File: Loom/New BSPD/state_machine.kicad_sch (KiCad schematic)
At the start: 9 parts, among them U1 4011, U11 4012, U12 74LS573, U3 4011, U4 4011, U5 4011, U6 4011, U7 4011, U8 4011

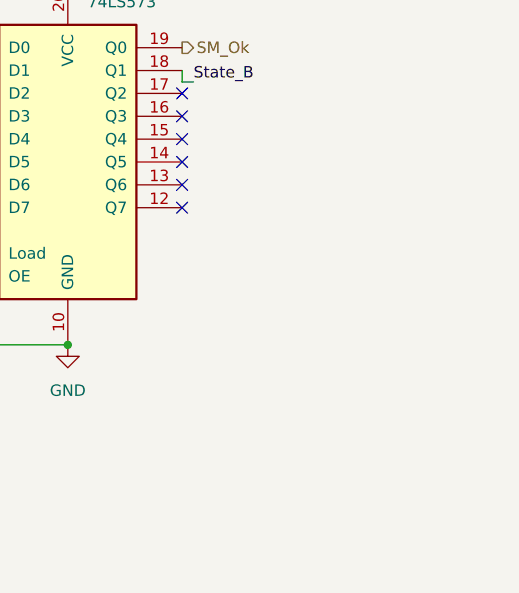
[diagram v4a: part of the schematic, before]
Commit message: Add State, Shutdown LEDs, Complete rough board layout
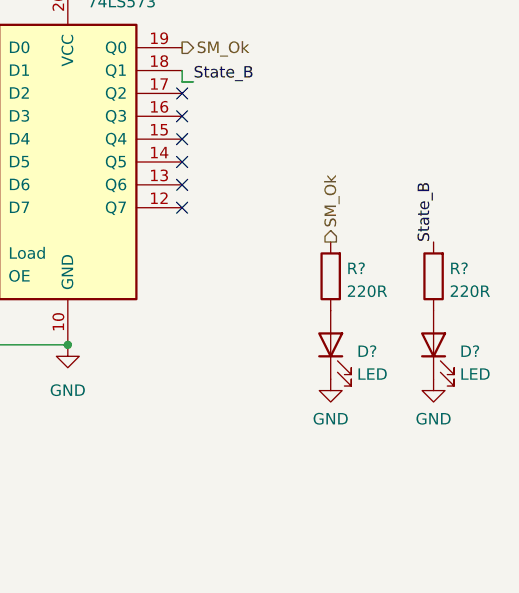
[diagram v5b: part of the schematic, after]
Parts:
- added D? (x2): LED, LED_THT:LED_D5.0mm, symbol Device:LED
- added R? (x2): 220R, Resistor_THT:R_Axial_DIN0207_L6.3mm_D2.5mm_P7.62mm_Horizontal, symbol Device:R
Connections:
- net GND: now also D?.1 (K), D?.1 (K)
- net SM_Ok: now also R?.2
- net State_B: now also R?.2
- new net: D?.2 (A), R?.1 (x2)
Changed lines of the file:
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@@
     (effects (font (size 1.27 1.27)) (justify right bottom))
+  )
+  (label "State_B" (at 264.16 72.39 90) (fields_autoplaced)
+    (effects (font (size 1.27 1.27)) (justify left bottom))
   )
   (label "State_B" (at 113.03 71.12 180) (fields_autoplaced)
@@
     (effects (font (size 1.27 1.27)) (justify right))
   )
+  (hierarchical_label "SM_Ok" (shape output) (at 252.73 72.39 90) (fields_autoplaced)
+    (effects (font (size 1.27 1.27)) (justify left))
+  )
   (hierarchical_label "SM_Ok" (shape output) (at 113.03 74.93 180) (fields_autoplaced)
     (effects (font (size 1.27 1.27)) (justify right))
@@
     )
   )
+  (symbol (lib_id "Device:R") (at 252.73 76.2 180) (unit 1)
+    (in_bom yes) (on_board yes) (dnp no) (fields_autoplaced)
+    (property "Reference" "R?" (at 254.508 75.3653 0)
+      (effects (font (size 1.27 1.27)) (justify right))
+    )
+    (property "Value" "220R" (at 254.508 77.9022 0)
+      (effects (font (size 1.27 1.27)) (justify right))
+    )
+    (property "Footprint" "Resistor_THT:R_Axial_DIN0207_L6.3mm_D2.5mm_P7.62mm_Horizontal" (at 254.508 76.2 90)
+      (effects (font (size 1.27 1.27)) hide)
+    )
+    (property "Datasheet" "~" (at 252.73 76.2 0)
+      (effects (font (size 1.27 1.27)) hide)
+    )
+    (pin "1")
+    (pin "2")
+    (instances
+      (project "New BSPD"
+        (path "/1f7c501a-057f-4634-92ce-528b01503799"
+          (reference "R?") (unit 1)
+        )
+        (path "/1f7c501a-057f-4634-92ce-528b01503799/81a2d232-b56a-457d-8f4d-f7bde46d944b"
+          (reference "R7") (unit 1)
+        )
+        (path "/1f7c501a-057f-4634-92ce-528b01503799/c1af1d02-f1c8-42b8-8d3c-ac3883e05aae"
+          (reference "R9") (unit 1)
+        )
+      )
+      (project "BSPD - FSG"
+        (path "/ea40ab7b-80c4-4cf6-acf9-83a05b0cd5a6"
+          (reference "R?") (unit 1)
+        )
+      )
+    )
+  )
   (symbol (lib_id "4xxx:4011") (at 55.88 139.7 0) (unit 4)
     (in_bom yes) (on_board yes) (dnp no) (fields_autoplaced)
@@
     )
   )
+  (symbol (lib_id "Device:LED") (at 264.16 83.82 90) (unit 1)
+    (in_bom yes) (on_board yes) (dnp no) (fields_autoplaced)
+    (property "Reference" "D?" (at 267.081 84.5728 90)
+      (effects (font (size 1.27 1.27)) (justify right))
+    )
+    (property "Value" "LED" (at 267.081 87.1097 90)
+      (effects (font (size 1.27 1.27)) (justify right))
+    )
+    (property "Footprint" "LED_THT:LED_D5.0mm" (at 264.16 83.82 0)
+      (effects (font (size 1.27 1.27)) hide)
+    )
+    (property "Datasheet" "~" (at 264.16 83.82 0)
+      (effects (font (size 1.27 1.27)) hide)
+    )
+    (pin "1")
+    (pin "2")
+    (instances
+      (project "New BSPD"
+        (path "/1f7c501a-057f-4634-92ce-528b01503799"
+          (reference "D?") (unit 1)
+        )
+        (path "/1f7c501a-057f-4634-92ce-528b01503799/81a2d232-b56a-457d-8f4d-f7bde46d944b"
+          (reference "D5") (unit 1)
+        )
+        (path "/1f7c501a-057f-4634-92ce-528b01503799/c1af1d02-f1c8-42b8-8d3c-ac3883e05aae"
+          (reference "D7") (unit 1)
+        )
+      )
+      (project "BSPD - FSG"
+        (path "/ea40ab7b-80c4-4cf6-acf9-83a05b0cd5a6"
+          (reference "D?") (unit 1)
+        )
+      )
+    )
+  )
   (symbol (lib_id "power:+5V") (at 171.45 21.59 0) (unit 1)
     (in_bom yes) (on_board yes) (dnp no) (fields_autoplaced)
@@
     )
   )
+  (symbol (lib_id "power:GND") (at 252.73 87.63 0) (unit 1)
+    (in_bom yes) (on_board yes) (dnp no) (fields_autoplaced)
+    (property "Reference" "#PWR?" (at 252.73 93.98 0)
+      (effects (font (size 1.27 1.27)) hide)
+    )
+    (property "Value" "GND" (at 252.73 92.0734 0)
+      (effects (font (size 1.27 1.27)))
+    )
+    (property "Footprint" "" (at 252.73 87.63 0)
+      (effects (font (size 1.27 1.27)) hide)
+    )
+    (property "Datasheet" "" (at 252.73 87.63 0)
+      (effects (font (size 1.27 1.27)) hide)
+    )
+    (pin "1")
+    (instances
+      (project "New BSPD"
+        (path "/1f7c501a-057f-4634-92ce-528b01503799"
+          (reference "#PWR?") (unit 1)
+        )
+        (path "/1f7c501a-057f-4634-92ce-528b01503799/81a2d232-b56a-457d-8f4d-f7bde46d944b"
+          (reference "#PWR022") (unit 1)
+        )
+        (path "/1f7c501a-057f-4634-92ce-528b01503799/c1af1d02-f1c8-42b8-8d3c-ac3883e05aae"
+          (reference "#PWR044") (unit 1)
+        )
+      )
+      (project "BSPD - FSG"
+        (path "/ea40ab7b-80c4-4cf6-acf9-83a05b0cd5a6"
+          (reference "#PWR?") (unit 1)
+        )
+      )
+    )
+  )
   (symbol (lib_id "power:+5V") (at 134.62 31.75 0) (unit 1)
     (in_bom yes) (on_board yes) (dnp no) (fields_autoplaced)
@@
     )
   )
+  (symbol (lib_id "Device:R") (at 264.16 76.2 180) (unit 1)
+    (in_bom yes) (on_board yes) (dnp no) (fields_autoplaced)
+    (property "Reference" "R?" (at 265.938 75.3653 0)
+      (effects (font (size 1.27 1.27)) (justify right))
+    )
+    (property "Value" "220R" (at 265.938 77.9022 0)
+      (effects (font (size 1.27 1.27)) (justify right))
+    )
+    (property "Footprint" "Resistor_THT:R_Axial_DIN0207_L6.3mm_D2.5mm_P7.62mm_Horizontal" (at 265.938 76.2 90)
+      (effects (font (size 1.27 1.27)) hide)
+    )
+    (property "Datasheet" "~" (at 264.16 76.2 0)
+      (effects (font (size 1.27 1.27)) hide)
+    )
+    (pin "1")
+    (pin "2")
+    (instances
+      (project "New BSPD"
+        (path "/1f7c501a-057f-4634-92ce-528b01503799"
+          (reference "R?") (unit 1)
+        )
+        (path "/1f7c501a-057f-4634-92ce-528b01503799/81a2d232-b56a-457d-8f4d-f7bde46d944b"
+          (reference "R7") (unit 1)
+        )
+        (path "/1f7c501a-057f-4634-92ce-528b01503799/c1af1d02-f1c8-42b8-8d3c-ac3883e05aae"
+          (reference "R10") (unit 1)
+        )
+      )
+      (project "BSPD - FSG"
+        (path "/ea40ab7b-80c4-4cf6-acf9-83a05b0cd5a6"
+          (reference "R?") (unit 1)
+        )
+      )
+    )
+  )
   (symbol (lib_id "4xxx:4011") (at 166.37 71.12 0) (unit 3)
     (in_bom yes) (on_board yes) (dnp no) (fields_autoplaced)
@@
     )
   )
+  (symbol (lib_id "power:GND") (at 264.16 87.63 0) (unit 1)
+    (in_bom yes) (on_board yes) (dnp no) (fields_autoplaced)
+    (property "Reference" "#PWR?" (at 264.16 93.98 0)
+      (effects (font (size 1.27 1.27)) hide)
+    )
+    (property "Value" "GND" (at 264.16 92.0734 0)
+      (effects (font (size 1.27 1.27)))
+    )
+    (property "Footprint" "" (at 264.16 87.63 0)
+      (effects (font (size 1.27 1.27)) hide)
+    )
+    (property "Datasheet" "" (at 264.16 87.63 0)
+      (effects (font (size 1.27 1.27)) hide)
+    )
+    (pin "1")
+    (instances
+      (project "New BSPD"
+        (path "/1f7c501a-057f-4634-92ce-528b01503799"
+          (reference "#PWR?") (unit 1)
+        )
+        (path "/1f7c501a-057f-4634-92ce-528b01503799/81a2d232-b56a-457d-8f4d-f7bde46d944b"
+          (reference "#PWR022") (unit 1)
+        )
+        (path "/1f7c501a-057f-4634-92ce-528b01503799/c1af1d02-f1c8-42b8-8d3c-ac3883e05aae"
+          (reference "#PWR045") (unit 1)
+        )
+      )
+      (project "BSPD - FSG"
+        (path "/ea40ab7b-80c4-4cf6-acf9-83a05b0cd5a6"
+          (reference "#PWR?") (unit 1)
+        )
+      )
+    )
+  )
   (symbol (lib_id "4xxx:4011") (at 101.6 66.04 0) (unit 4)
     (in_bom yes) (on_board yes) (dnp no) (fields_autoplaced)
@@
         )
       )
+    )
+  )
+  (symbol (lib_id "Device:LED") (at 252.73 83.82 90) (unit 1)
+    (in_bom yes) (on_board yes) (dnp no) (fields_autoplaced)
+    (property "Reference" "D?" (at 255.651 84.5728 90)
+      (effects (font (size 1.27 1.27)) (justify right))
+    )
+    (property "Value" "LED" (at 255.651 87.1097 90)
+      (effects (font (size 1.27 1.27)) (justify right))
+    )
+    (property "Footprint" "LED_THT:LED_D5.0mm" (at 252.73 83.82 0)
+      (effects (font (size 1.27 1.27)) hide)
+    )
+    (property "Datasheet" "~" (at 252.73 83.82 0)
+      (effects (font (size 1.27 1.27)) hide)
+    )
+    (pin "1")
+    (pin "2")
+    (instances
+      (project "New BSPD"
+        (path "/1f7c501a-057f-4634-92ce-528b01503799"
+          (reference "D?") (unit 1)
+        )
+        (path "/1f7c501a-057f-4634-92ce-528b01503799/81a2d232-b56a-457d-8f4d-f7bde46d944b"
+          (reference "D5") (unit 1)
+        )
+        (path "/1f7c501a-057f-4634-92ce-528b01503799/c1af1d02-f1c8-42b8-8d3c-ac3883e05aae"
+          (reference "D6") (unit 1)
+        )
+      )
+      (project "BSPD - FSG"
+        (path "/ea40ab7b-80c4-4cf6-acf9-83a05b0cd5a6"
+          (reference "D?") (unit 1)
+        )
+      )

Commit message: Complete New BSPD!
TODO: Decide if the crystal needs a capacitor or not
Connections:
- net at U5.3: now also U11.11; no longer U11.10
- net at U5.4: now also U11.10; no longer U11.11
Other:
- moved on the sheet: U5A, U5B, U5D
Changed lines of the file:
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@@
     (stroke (width 0) (type default))
   )
-  (wire (pts (xy 109.22 66.04) (xy 113.03 66.04))
+  (wire (pts (xy 109.22 74.93) (xy 113.03 74.93))
     (stroke (width 0) (type default))
   )
@@
     (stroke (width 0) (type default))
   )
+  (wire (pts (xy 109.22 52.07) (xy 113.03 52.07))
+    (stroke (width 0) (type default))
+  )
+  (wire (pts (xy 129.54 68.58) (xy 129.54 74.93))
+    (stroke (width 0) (type default))
+  )
+  (wire (pts (xy 129.54 46.99) (xy 135.89 46.99))
+    (stroke (width 0) (type default))
+  )
+  (wire (pts (xy 158.75 48.26) (xy 158.75 55.88))
+    (stroke (width 0) (type default))
+  )
+  (wire (pts (xy 92.71 77.47) (xy 93.98 77.47))
+    (stroke (width 0) (type default))
+  )
+  (wire (pts (xy 129.54 58.42) (xy 128.27 58.42))
+    (stroke (width 0) (type default))
+  )
+  (wire (pts (xy 129.54 86.36) (xy 128.27 86.36))
+    (stroke (width 0) (type default))
+  )
+  (wire (pts (xy 93.98 72.39) (xy 92.71 72.39))
+    (stroke (width 0) (type default))
+  )
+  (wire (pts (xy 208.28 50.8) (xy 208.28 40.64))
+    (stroke (width 0) (type default))
+  )
+  (wire (pts (xy 236.22 54.61) (xy 236.22 53.34))
+    (stroke (width 0) (type default))
+  )
+  (wire (pts (xy 63.5 139.7) (xy 63.5 137.16))
+    (stroke (width 0) (type default))
+  )
+  (wire (pts (xy 151.13 76.2) (xy 177.8 76.2))
+    (stroke (width 0) (type default))
+  )
   (wire (pts (xy 128.27 77.47) (xy 135.89 77.47))
     (stroke (width 0) (type default))
   )
-  (wire (pts (xy 109.22 52.07) (xy 113.03 52.07))
-    (stroke (width 0) (type default))
-  )
-  (wire (pts (xy 129.54 46.99) (xy 135.89 46.99))
-    (stroke (width 0) (type default))
-  )
-  (wire (pts (xy 158.75 48.26) (xy 158.75 55.88))
-    (stroke (width 0) (type default))
-  )
-  (wire (pts (xy 92.71 68.58) (xy 93.98 68.58))
-    (stroke (width 0) (type default))
-  )
-  (wire (pts (xy 129.54 58.42) (xy 128.27 58.42))
-    (stroke (width 0) (type default))
-  )
-  (wire (pts (xy 129.54 86.36) (xy 128.27 86.36))
-    (stroke (width 0) (type default))
-  )
-  (wire (pts (xy 93.98 63.5) (xy 92.71 63.5))
-    (stroke (width 0) (type default))
-  )
-  (wire (pts (xy 208.28 50.8) (xy 208.28 40.64))
-    (stroke (width 0) (type default))
-  )
-  (wire (pts (xy 236.22 54.61) (xy 236.22 53.34))
-    (stroke (width 0) (type default))
-  )
-  (wire (pts (xy 63.5 139.7) (xy 63.5 137.16))
-    (stroke (width 0) (type default))
-  )
-  (wire (pts (xy 151.13 76.2) (xy 177.8 76.2))
+  (wire (pts (xy 129.54 74.93) (xy 135.89 74.93))
     (stroke (width 0) (type default))
   )
@@
     (stroke (width 0) (type default))
   )
-  (wire (pts (xy 129.54 74.93) (xy 135.89 74.93))
-    (stroke (width 0) (type default))
-  )
   (wire (pts (xy 193.04 43.18) (xy 193.04 48.26))
     (stroke (width 0) (type default))
@@
     (stroke (width 0) (type default))
   )
+  (wire (pts (xy 92.71 72.39) (xy 92.71 77.47))
+    (stroke (width 0) (type default))
+  )
   (wire (pts (xy 128.27 68.58) (xy 129.54 68.58))
     (stroke (width 0) (type default))
   )
-  (wire (pts (xy 92.71 63.5) (xy 92.71 68.58))
-    (stroke (width 0) (type default))
-  )
   (wire (pts (xy 173.99 71.12) (xy 177.8 71.12))
     (stroke (width 0) (type default))
@@
   )
   (wire (pts (xy 193.04 68.58) (xy 193.04 73.66))
-    (stroke (width 0) (type default))
-  )
-  (wire (pts (xy 129.54 68.58) (xy 129.54 74.93))
     (stroke (width 0) (type default))
   )
@@
     (effects (font (size 1.27 1.27)) (justify left bottom))
   )
-  (label "State_B" (at 113.03 71.12 180) (fields_autoplaced)
+  (label "State_B" (at 113.03 80.01 180) (fields_autoplaced)
     (effects (font (size 1.27 1.27)) (justify right bottom))
   )
@@
     (effects (font (size 1.27 1.27)) (justify left))
   )
-  (hierarchical_label "SM_Ok" (shape output) (at 113.03 74.93 180) (fields_autoplaced)
+  (hierarchical_label "SM_Ok" (shape output) (at 113.03 66.04 180) (fields_autoplaced)
     (effects (font (size 1.27 1.27)) (justify right))
   )
@@
     (effects (font (size 1.27 1.27)) (justify right))
   )
-  (hierarchical_label "System_OK" (shape input) (at 113.03 80.01 180) (fields_autoplaced)
+  (hierarchical_label "System_OK" (shape input) (at 113.03 71.12 180) (fields_autoplaced)
     (effects (font (size 1.27 1.27)) (justify right))
   )
@@
     (effects (font (size 1.27 1.27)) (justify right))
   )
-  (hierarchical_label "SM_Ok" (shape output) (at 92.71 66.04 180) (fields_autoplaced)
+  (hierarchical_label "SM_Ok" (shape output) (at 92.71 74.93 180) (fields_autoplaced)
     (effects (font (size 1.27 1.27)) (justify right))
   )
@@
     (effects (font (size 1.27 1.27)) (justify right))
   )
-  (symbol (lib_id "4xxx:4011") (at 120.65 68.58 0) (unit 1)
-    (in_bom yes) (on_board yes) (dnp no) (fields_autoplaced)
-    (property "Reference" "U5" (at 120.6417 59.69 0)
-      (effects (font (size 1.27 1.27)))
-    )
-    (property "Value" "4011" (at 120.6417 62.23 0)
-      (effects (font (size 1.27 1.27)))
-    )
-    (property "Footprint" "Package_DIP:DIP-14_W7.62mm_Socket" (at 120.65 68.58 0)
-      (effects (font (size 1.27 1.27)) hide)
-    )
-    (property "Datasheet" "http://www.intersil.com/content/dam/Intersil/documents/cd40/cd4011bms-12bms-23bms.pdf" (at 120.65 68.58 0)
+  (symbol (lib_id "4xxx:4011") (at 120.65 77.47 0) (unit 1)
+    (in_bom yes) (on_board yes) (dnp no) (fields_autoplaced)
+    (property "Reference" "U5" (at 120.6417 68.58 0)
+      (effects (font (size 1.27 1.27)))
+    )
+    (property "Value" "4011" (at 120.6417 71.12 0)
+      (effects (font (size 1.27 1.27)))
+    )
+    (property "Footprint" "Package_DIP:DIP-14_W7.62mm_Socket" (at 120.65 77.47 0)
+      (effects (font (size 1.27 1.27)) hide)
+    )
+    (property "Datasheet" "http://www.intersil.com/content/dam/Intersil/documents/cd40/cd4011bms-12bms-23bms.pdf" (at 120.65 77.47 0)
       (effects (font (size 1.27 1.27)) hide)
     )
@@
     )
   )
-  (symbol (lib_id "4xxx:4011") (at 120.65 77.47 0) (unit 2)
-    (in_bom yes) (on_board yes) (dnp no) (fields_autoplaced)
-    (property "Reference" "U5" (at 120.6417 68.58 0)
-      (effects (font (size 1.27 1.27)))
-    )
-    (property "Value" "4011" (at 120.6417 71.12 0)
-      (effects (font (size 1.27 1.27)))
-    )
-    (property "Footprint" "Package_DIP:DIP-14_W7.62mm_Socket" (at 120.65 77.47 0)
-      (effects (font (size 1.27 1.27)) hide)
-    )
-    (property "Datasheet" "http://www.intersil.com/content/dam/Intersil/documents/cd40/cd4011bms-12bms-23bms.pdf" (at 120.65 77.47 0)
+  (symbol (lib_id "4xxx:4011") (at 120.65 68.58 0) (unit 2)
+    (in_bom yes) (on_board yes) (dnp no) (fields_autoplaced)
+    (property "Reference" "U5" (at 120.6417 59.69 0)
+      (effects (font (size 1.27 1.27)))
+    )
+    (property "Value" "4011" (at 120.6417 62.23 0)
+      (effects (font (size 1.27 1.27)))
+    )
+    (property "Footprint" "Package_DIP:DIP-14_W7.62mm_Socket" (at 120.65 68.58 0)
+      (effects (font (size 1.27 1.27)) hide)
+    )
+    (property "Datasheet" "http://www.intersil.com/content/dam/Intersil/documents/cd40/cd4011bms-12bms-23bms.pdf" (at 120.65 68.58 0)
       (effects (font (size 1.27 1.27)) hide)
     )
@@
     )
   )
-  (symbol (lib_id "4xxx:4011") (at 101.6 66.04 0) (unit 4)
-    (in_bom yes) (on_board yes) (dnp no) (fields_autoplaced)
-    (property "Reference" "U5" (at 101.5917 57.15 0)
-      (effects (font (size 1.27 1.27)))
-    )
-    (property "Value" "4011" (at 101.5917 59.69 0)
-      (effects (font (size 1.27 1.27)))
-    )
-    (property "Footprint" "Package_DIP:DIP-14_W7.62mm_Socket" (at 101.6 66.04 0)
-      (effects (font (size 1.27 1.27)) hide)
-    )
-    (property "Datasheet" "http://www.intersil.com/content/dam/Intersil/documents/cd40/cd4011bms-12bms-23bms.pdf" (at 101.6 66.04 0)
-      (effects (font (size 1.27 1.27)) hide)
-    )
+  (symbol (lib_id "4xxx:4011") (at 101.6 74.93 0) (unit 4)
+    (in_bom yes) (on_board yes) (dnp no) (fields_autoplaced)
+    (property "Reference" "U5" (at 101.5917 66.04 0)
+      (effects (font (size 1.27 1.27)))
+    )
+    (property "Value" "4011" (at 101.5917 68.58 0)
+      (effects (font (size 1.27 1.27)))
+    )
+    (property "Footprint" "Package_DIP:DIP-14_W7.62mm_Socket" (at 101.6 74.93 0)
+      (effects (font (size 1.27 1.27)) hide)
+    )
+    (property "Datasheet" "http://www.intersil.com/content/dam/Intersil/documents/cd40/cd4011bms-12bms-23bms.pdf" (at 101.6 74.93 0)
+      (effects (font (size 1.27 1.27)) hide)
+    )
